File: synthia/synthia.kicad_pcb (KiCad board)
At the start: 4 copper layers, 285 x 257.5 mm, 165 parts, among them J1 MJ-63022B, J2 SJ3-35083C-TR, J3 PJ-007, J4 SDS-50J, Q1 IRF9540N, U1 TLV272IP, U2 STM32H750ZBT6, U3 LD1117V33

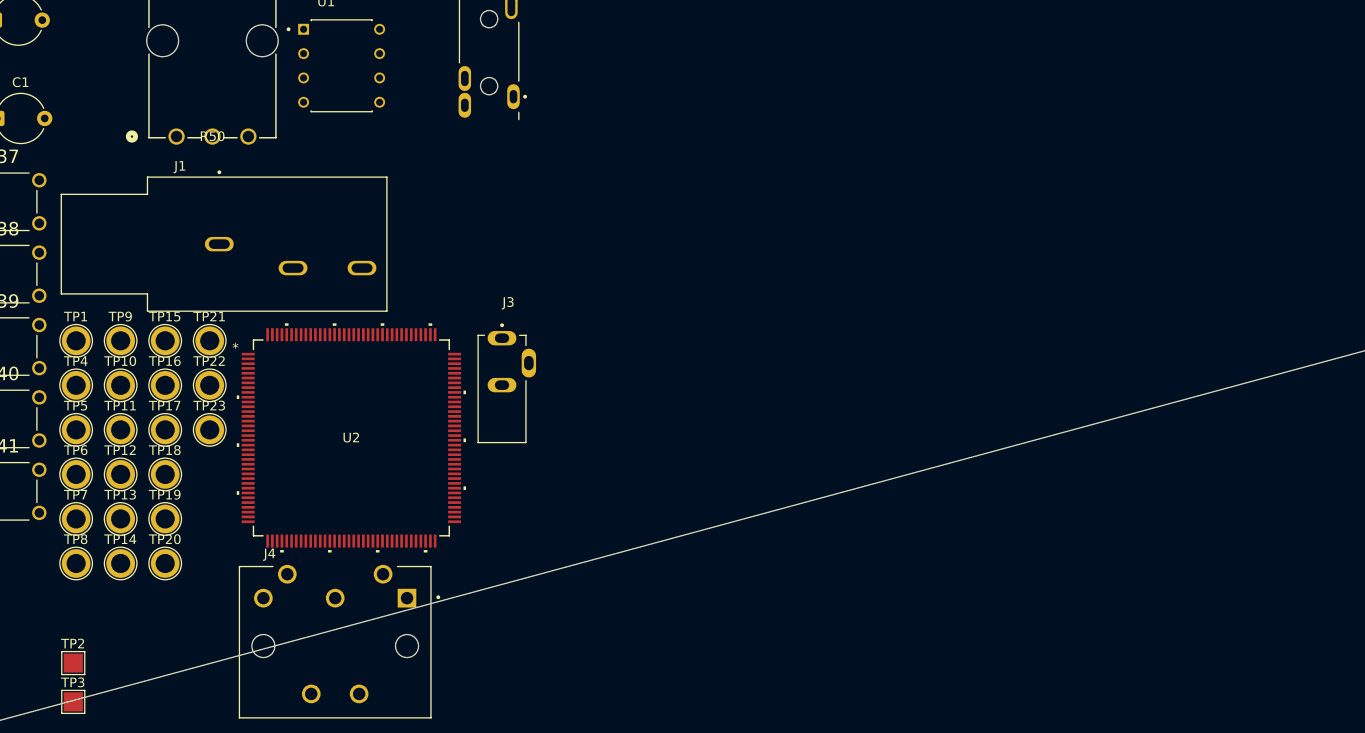
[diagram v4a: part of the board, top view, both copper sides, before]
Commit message: More changes made during Jank. Made a symbol and footprint for the latching switch
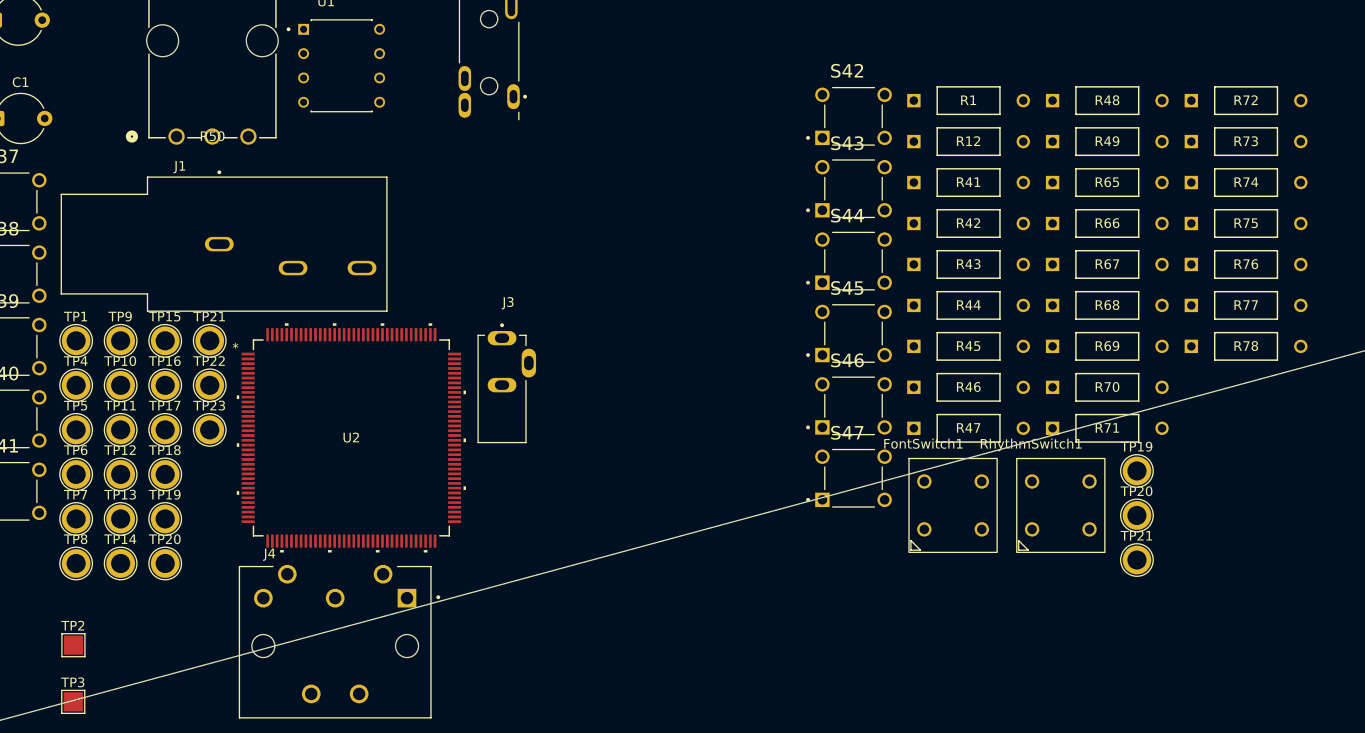
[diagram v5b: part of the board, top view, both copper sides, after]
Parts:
- added FontSwitch1: ~, Synthia_footprint_library:Latching Switch, F.Cu at (265.7, 117.0)
- added R1: 100kΩ, Synthia_footprint_library:STA_CF14_STP, F.Cu at (266.2, 79.6)
- added R12: 100kΩ, Synthia_footprint_library:STA_CF14_STP, F.Cu at (266.2, 83.9)
- added R41: 100kΩ, Synthia_footprint_library:STA_CF14_STP, F.Cu at (266.2, 88.2)
- added R42: 100kΩ, Synthia_footprint_library:STA_CF14_STP, F.Cu at (266.2, 92.5)
- added R43: 100kΩ, Synthia_footprint_library:STA_CF14_STP, F.Cu at (266.2, 96.7)
- added R44: 100kΩ, Synthia_footprint_library:STA_CF14_STP, F.Cu at (266.2, 101.0)
- added R45: 100kΩ, Synthia_footprint_library:STA_CF14_STP, F.Cu at (266.2, 105.3)
- added R46: 100kΩ, Synthia_footprint_library:STA_CF14_STP, F.Cu at (266.2, 109.6)
- added R47: 100kΩ, Synthia_footprint_library:STA_CF14_STP, F.Cu at (266.2, 113.9)
- added R48: 100kΩ, Synthia_footprint_library:STA_CF14_STP, F.Cu at (280.7, 79.6)
- added R49: 100kΩ, Synthia_footprint_library:STA_CF14_STP, F.Cu at (280.7, 83.9)
- added R65: 100k, Synthia_footprint_library:STA_CF14_STP, F.Cu at (280.7, 88.2)
- added R66: 100k, Synthia_footprint_library:STA_CF14_STP, F.Cu at (280.7, 92.5)
- added R67: 100k, Synthia_footprint_library:STA_CF14_STP, F.Cu at (280.7, 96.7)
- added R68: 100k, Synthia_footprint_library:STA_CF14_STP, F.Cu at (280.7, 101.0)
- added R69: 100k, Synthia_footprint_library:STA_CF14_STP, F.Cu at (280.7, 105.3)
- added R70: 100k, Synthia_footprint_library:STA_CF14_STP, F.Cu at (280.7, 109.6)
- added R71: 100k, Synthia_footprint_library:STA_CF14_STP, F.Cu at (280.7, 113.9)
- added R72: 100k, Synthia_footprint_library:STA_CF14_STP, F.Cu at (295.2, 79.6)
- added R73: 100k, Synthia_footprint_library:STA_CF14_STP, F.Cu at (295.2, 83.9)
- added R74: 100k, Synthia_footprint_library:STA_CF14_STP, F.Cu at (295.2, 88.2)
- added R75: 100k, Synthia_footprint_library:STA_CF14_STP, F.Cu at (295.2, 92.5)
- added R76: 100k, Synthia_footprint_library:STA_CF14_STP, F.Cu at (295.2, 96.7)
- added R77: 100k, Synthia_footprint_library:STA_CF14_STP, F.Cu at (295.2, 101.0)
- added R78: 100k, Synthia_footprint_library:STA_CF14_STP, F.Cu at (295.2, 105.3)
- added RhythmSwitch1: ~, Synthia_footprint_library:Latching Switch, F.Cu at (277.0, 117.0)
- added S42: RESET, Synthia_footprint_library:SW_TL1105BF160Q, F.Cu at (259.9, 81.3)
- added S43: TL1105BF160Q, Synthia_footprint_library:SW_TL1105BF160Q, F.Cu at (259.9, 88.8)
- added S44: TL1105BF160Q, Synthia_footprint_library:SW_TL1105BF160Q, F.Cu at (259.9, 96.4)
- added S45: TL1105BF160Q, Synthia_footprint_library:SW_TL1105BF160Q, F.Cu at (259.9, 104.0)
- added S46: TL1105BF160Q, Synthia_footprint_library:SW_TL1105BF160Q, F.Cu at (259.9, 111.5)
- added S47: TL1105BF160Q, Synthia_footprint_library:SW_TL1105BF160Q, F.Cu at (259.9, 119.1)
- added TP19: MicroUSB D- Pin, TestPoint:TestPoint_Plated_Hole_D2.0mm, F.Cu at (289.5, 118.3)
- added TP20: MicroUSB D+ Pin, TestPoint:TestPoint_Plated_Hole_D2.0mm, F.Cu at (289.5, 123.0)
- added TP21: MicroUSB GND, TestPoint:TestPoint_Plated_Hole_D2.0mm, F.Cu at (289.5, 127.6)
- moved TP2 1.87 mm to (178.5, 136.5)
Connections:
- U2 pad 100: /Button_Matrix/ScanCol5 -> unconnected-(U2B-PA8-Pad100)
- U2 pad 101: /Button_Matrix/ScanCol4 -> unconnected-(U2B-PA9-Pad101)
- U2 pad 102: /Button_Matrix/ScanCol3 -> unconnected-(U2B-PA10-Pad102)
- U2 pad 103: /Button_Matrix/ScanCol2 -> Net-(U2B-PA11)
- U2 pad 104: /Button_Matrix/ScanCol1 -> Net-(U2B-PA12)
- U2 pad 105: /Button_Matrix/ScanCol0 -> unconnected-(U2B-PA13-Pad105)
- U2 pad 111: /Button_Matrix/ScanRow0 -> unconnected-(U2B-PC10-Pad111)
- U2 pad 112: /Button_Matrix/ScanRow1 -> unconnected-(U2B-PC11-Pad112)
- U2 pad 113: /Button_Matrix/ScanRow2 -> unconnected-(U2B-PC12-Pad113)
- U2 pad 25: unconnected-(U2A-NRST-Pad25) -> Net-(U2A-NRST)
- U2 pad 92: /Button_Matrix/ScanCol11 -> unconnected-(U2B-PG7-Pad92)
- U2 pad 93: /Button_Matrix/ScanCol10 -> unconnected-(U2B-PG8-Pad93)
- U2 pad 96: /Button_Matrix/ScanCol9 -> unconnected-(U2B-PC6-Pad96)
- U2 pad 97: /Button_Matrix/ScanCol8 -> unconnected-(U2B-PC7-Pad97)
- U2 pad 98: /Button_Matrix/ScanCol7 -> unconnected-(U2B-PC8-Pad98)
- U2 pad 99: /Button_Matrix/ScanCol6 -> unconnected-(U2B-PC69-Pad99)

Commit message: did some pcb work, initial wiring complete
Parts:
- moved U2 139.8 mm to (297.1, 222.2), turned to -90 degrees
- moved TP19 127.0 mm to (303.7, 244.5), turned to 90 degrees
- moved TP20 123.3 mm to (310.1, 244.5), turned to 90 degrees
- moved TP21 120.3 mm to (316.8, 244.8), turned to 90 degrees
- moved R1 104.4 mm to (349.5, 142.6)
- moved R12 104.4 mm to (349.5, 146.9)
- moved R41 104.4 mm to (349.5, 151.2)
- moved R42 104.4 mm to (349.5, 155.5)
- moved R43 104.4 mm to (349.5, 159.7)
- moved R44 104.4 mm to (349.5, 164.0)
- moved R45 104.4 mm to (349.5, 168.3)
- moved S42 104.4 mm to (343.2, 144.3)
- moved S43 104.4 mm to (343.2, 151.8)
- moved S44 104.4 mm to (343.2, 159.4)
- moved S46 104.4 mm to (343.2, 174.5)
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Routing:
- net /Button_Matrix/ScanRow2: track 0.00 -> 271.4 mm, vias 0 -> 22
- net /Button_Matrix/ScanRow1: track 0.00 -> 253.3 mm, vias 0 -> 22
- net /Button_Matrix/ScanRow0: track 0.00 -> 251.0 mm, vias 0 -> 22
- net /Button_Matrix/ScanCol1: track 0.00 -> 92.6 mm
- net /Button_Matrix/ScanCol3: track 0.00 -> 92.5 mm
- net /Button_Matrix/ScanCol5: track 0.00 -> 92.5 mm
- net /Button_Matrix/ScanCol10: track 0.00 -> 92.5 mm
- net /Button_Matrix/ScanCol0: track 0.00 -> 92.4 mm
- net /Button_Matrix/ScanCol7: track 0.00 -> 92.4 mm
- net /Button_Matrix/ScanCol2: track 0.00 -> 92.4 mm
- net /Button_Matrix/ScanCol9: track 0.00 -> 92.4 mm
- net /Button_Matrix/ScanCol8: track 0.00 -> 92.4 mm
- net /Button_Matrix/ScanCol11: track 0.00 -> 92.3 mm
- net /Button_Matrix/ScanCol4: track 0.00 -> 92.3 mm
- net /Button_Matrix/ScanCol6: track 0.00 -> 92.3 mm
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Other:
- board size 285 x 257.5 mm -> 300 x 271.1 mm
- copper layers 4 -> 2
- board text added: "D+"
- board text added: "D-"
- board text added: "GND"
- board text added: "ScanRow0"
- board text added: "ScanRow1"
- board text added: "ScanRow2"

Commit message: Continued on PCB design and wiring, cannot continue until design has been further completed
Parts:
- moved C2 229.4 mm to (386.5, 171.2)
- moved C3 223.5 mm to (384.2, 158.2), turned to 180 degrees
- moved TP1 219.8 mm to (390.8, 158.2), turned to 90 degrees
- moved TP15 210.9 mm to (390.8, 148.9), turned to 90 degrees
- moved C1 210.2 mm to (370.2, 174.5)
- moved TP19 210.2 mm to (387.8, 216.3)
- moved TP2 210.2 mm to (378.2, 229.5)
- moved TP20 210.2 mm to (387.8, 220.9)
- moved TP4 210.2 mm to (378.5, 202.3)
- moved TP5 210.2 mm to (378.5, 207.0)
- moved TP6 210.2 mm to (378.5, 211.6)
- moved TP7 210.2 mm to (378.5, 216.3)
- moved TP8 210.2 mm to (378.5, 220.9)
- moved U3 210.2 mm to (365.2, 229.0)
- moved R2 210.2 mm to (353.0, 161.5)
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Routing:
- net /DAC_schematic/OUT: track 0.00 -> 125.7 mm
- net Net-(U1-1IN+): track 0.00 -> 84.1 mm, vias 0 -> 2
- net /DAC_schematic/DAC7: track 0.00 -> 81.2 mm
- net /DAC_schematic/DAC6: track 0.00 -> 81.0 mm
- net /DAC_schematic/DAC3: track 0.00 -> 80.6 mm
- net /DAC_schematic/DAC0: track 0.00 -> 80.6 mm
- net /DAC_schematic/DAC1: track 0.00 -> 80.6 mm
- net /DAC_schematic/DAC5: track 0.00 -> 80.5 mm
- net /DAC_schematic/DAC4: track 0.00 -> 80.5 mm
- net /DAC_schematic/DAC2: track 0.00 -> 80.4 mm
- net Net-(U1-2IN-): track 0.00 -> 53.2 mm
- net Net-(U1-1OUT): track 0.00 -> 47.8 mm, vias 0 -> 2
- net Net-(J4-Pad2): track 0.00 -> 38.0 mm
- net Net-(J4-Pad4): track 0.00 -> 35.6 mm
- net Net-(U1-1IN-): track 0.00 -> 29.6 mm
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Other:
- board text added: "SHIELD / GROUND"
- board text added: "SINK"
- board text added: "SOURCE"
- board text added: "SPEAKER GND"
- board text added: "SPEAKER PWR"

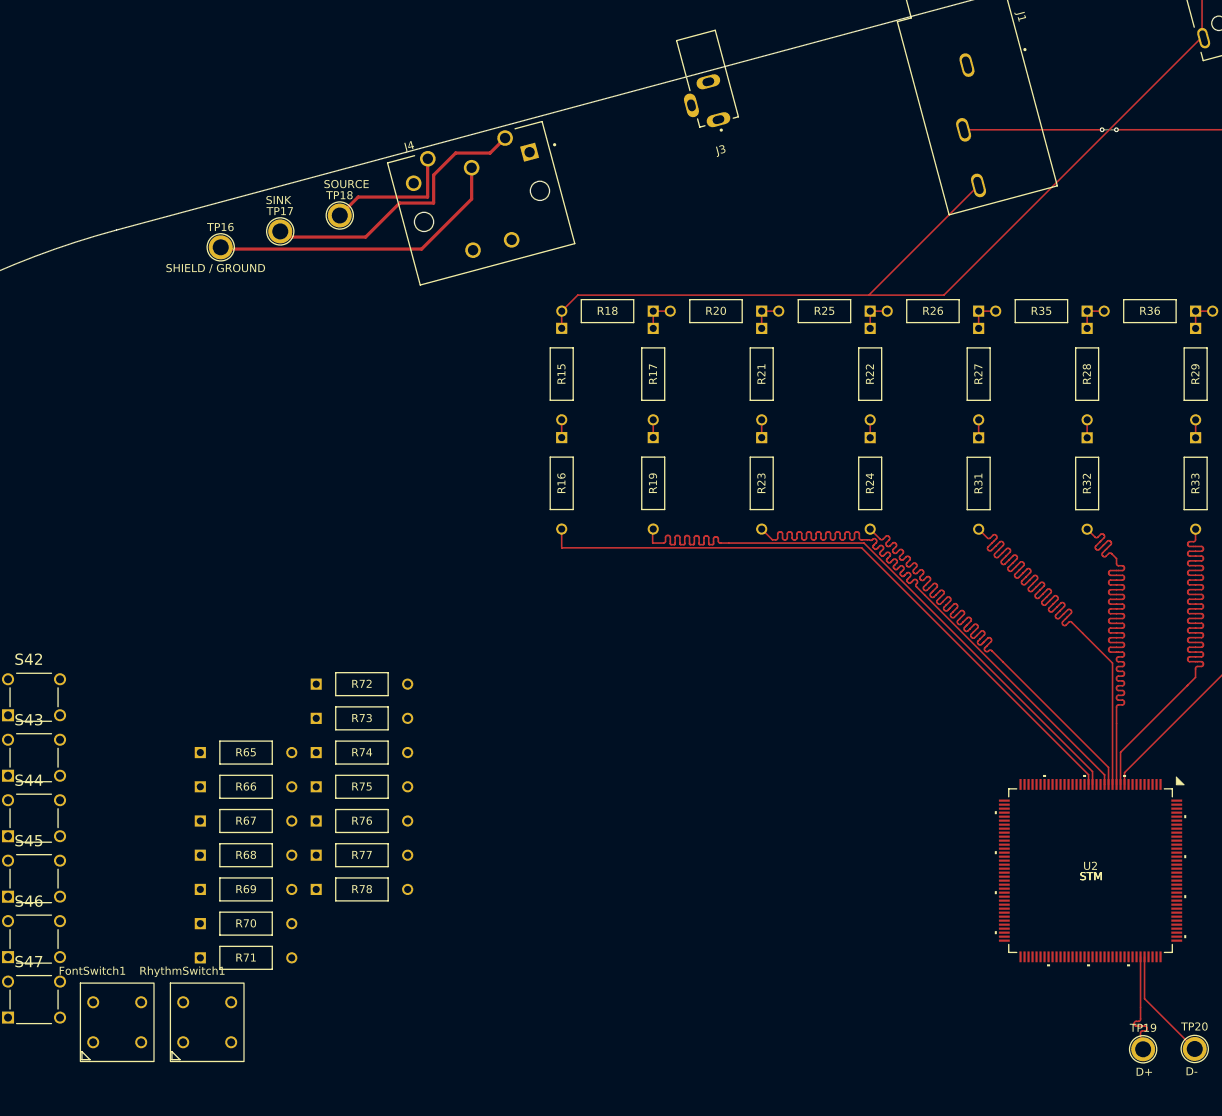
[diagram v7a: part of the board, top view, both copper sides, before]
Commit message: added all 3D models for the footprints into the pcb design, fixed some DRC errors
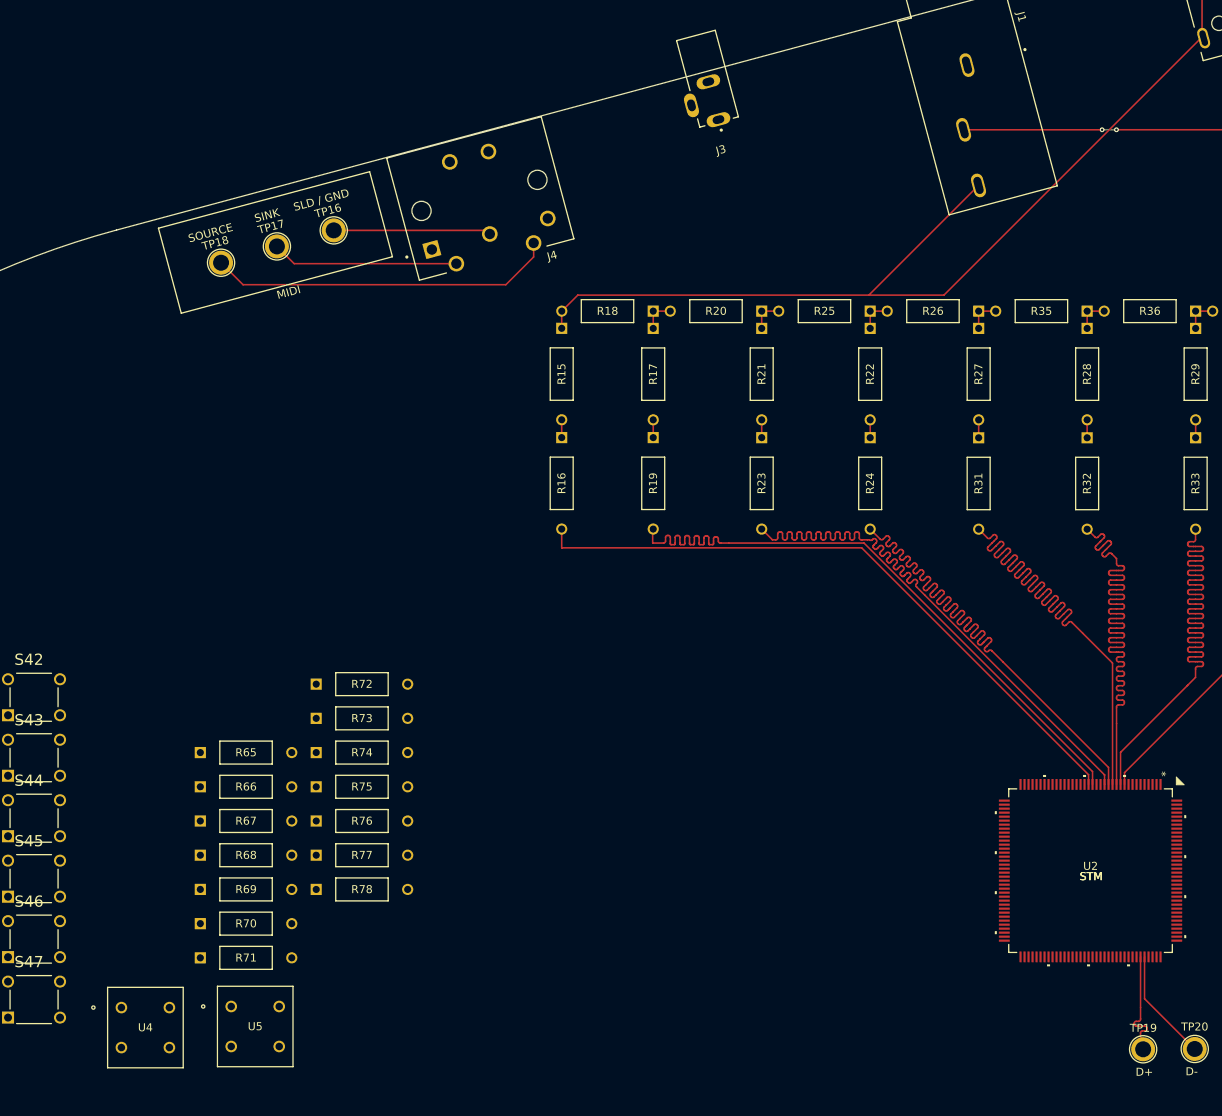
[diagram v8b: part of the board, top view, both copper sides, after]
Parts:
- removed FontSwitch1, RhythmSwitch1: ~, Synthia_footprint_library:Latching Switch
- added U4: PVA1EEH31.2NV2, Synthia_footprint_library:SWITCH_H31.2NV2, F.Cu at (176.0, 239.3)
- added U5: PVA1EEH31.2NV2, Synthia_footprint_library:SWITCH_H31.2NV2, F.Cu at (189.7, 239.2)
- moved TP18 16.0 mm to (188.4, 146.2)
- moved TP16 14.3 mm to (202.5, 142.2)
- moved TP17 1.92 mm to (195.4, 144.2)
- moved J4 1.41 mm to (220.7, 137.8), turned to -165 degrees
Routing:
- net Net-(J4-Pad5): track 16.7 -> 43.4 mm
- net Net-(J4-Pad2): track 38.0 -> 19.7 mm
- net Net-(J4-Pad4): track 35.6 -> 23.3 mm
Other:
- board text added: "MIDI"
- board text added: "SLD / GND"
- board text removed: "SHIELD / GROUND"
